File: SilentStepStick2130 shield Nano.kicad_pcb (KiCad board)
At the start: 4 copper layers, 34.5 x 49.4 mm, 8 parts, among them J1 Conn_01x04_Socket, J2 Conn_01x04_Socket, J5 Conn_01x03, U1 TMC2130_SILENTSTEPSTICK, U2 TMC2130_SILENTSTEPSTICK

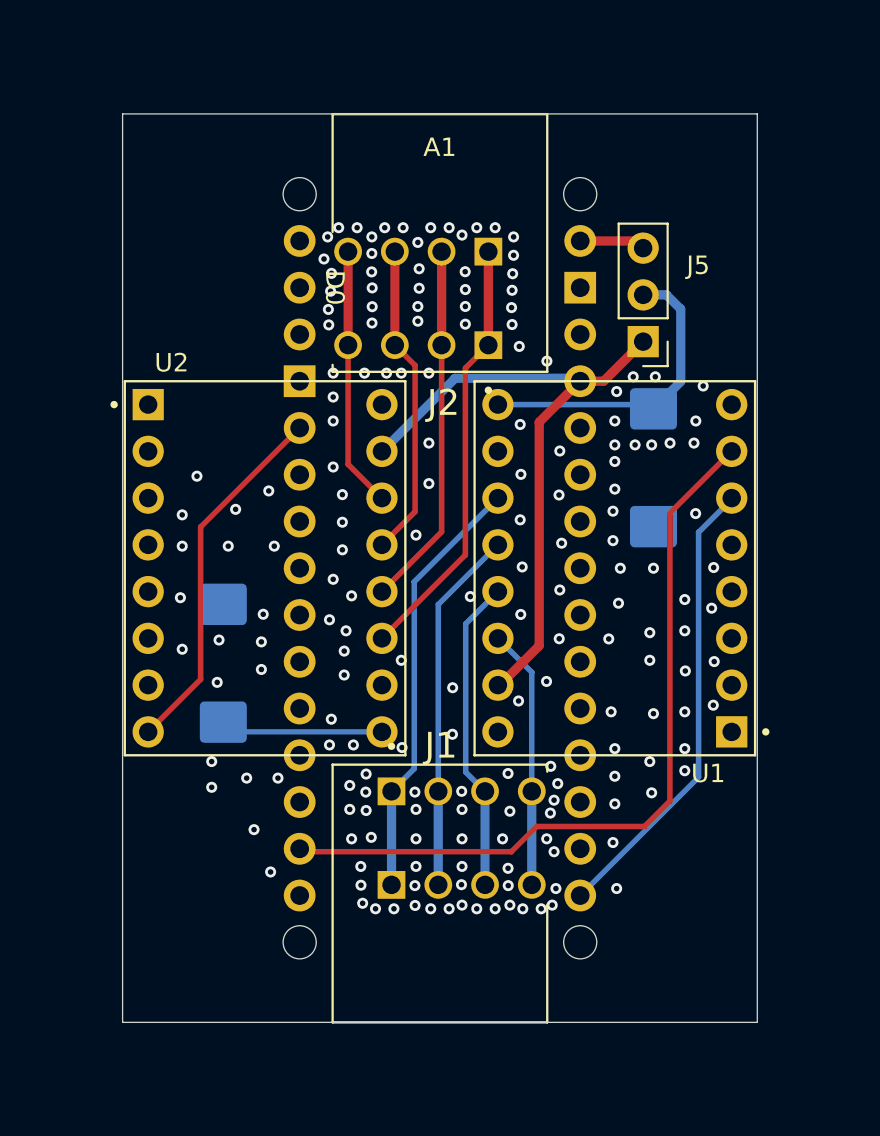
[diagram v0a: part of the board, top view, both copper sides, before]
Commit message: redo, nano on the wrong side (can work with headerless nano)
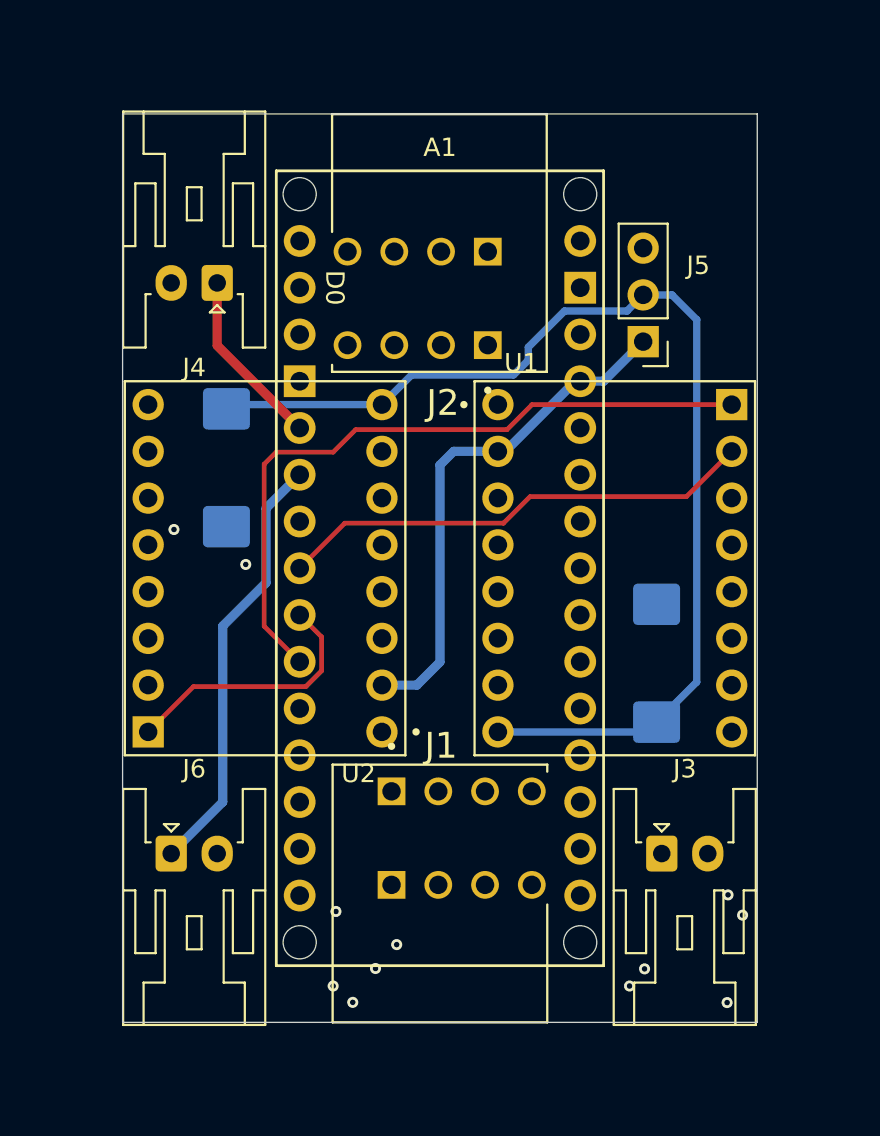
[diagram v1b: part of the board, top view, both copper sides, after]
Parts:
- added J3: Conn_01x02_Pin, Connector_JST:JST_XA_S02B-XASK-1_1x02_P2.50mm_Horizontal, F.Cu at (162.1, 115.5)
- added J4: Conn_01x02_Pin, Connector_JST:JST_XA_S02B-XASK-1_1x02_P2.50mm_Horizontal, F.Cu at (137.9, 84.5)
- added J6: Conn_01x02_Pin, Connector_JST:JST_XA_S02B-XASK-1_1x02_P2.50mm_Horizontal, F.Cu at (135.4, 115.5)
- A1: footprint LibPersoNadj:Arduino_Nano_Every_Shield -> PCM_arduino-library:Arduino_Nano_Every_Socket
- moved C1 23.5 mm to (161.8, 105.2)
- moved C2 23.2 mm to (138.4, 94.5)
- moved A1 21.6 mm to (150.0, 121.6)
- turned U1 to 0 degrees
- turned U2 to 180 degrees
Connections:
- A1 pad D10: unconnected-(A1-PadD10) -> /CS_1
- A1 pad D2: /~{EN_2} -> Net-(J4-Pin_1)
- A1 pad D3: /~{EN_1} -> Net-(J6-Pin_1)
- A1 pad D8: /CS_2 -> Net-(J3-Pin_1)
- A1 pad D9: /CS_1 -> /CS_2
- U1 pad 8: /~{EN_1} -> GND
- U2 pad 8: /~{EN_2} -> GND
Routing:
- net Net-(J3-Pin_1): track 0.00 -> 37.9 mm, vias 0 -> 2
- net /CS_1: track 30.6 -> 58.1 mm, vias 0 -> 2
- net /~{EN_1}: track 26.4 -> 0.00 mm
- net Net-(J6-Pin_1): track 0.00 -> 23.5 mm
- net /~{EN_2}: track 19.9 -> 0.00 mm
- net /VM: track 46.2 -> 60.7 mm
- net /DIR_1: track 25.0 -> 38.3 mm
- net /MISO: track 61.9 -> 75.0 mm, vias 0 -> 2
- net /SCK: track 56.2 -> 68.6 mm, vias 0 -> 2
- net /MOSI: track 55.8 -> 66.8 mm, vias 0 -> 2
- net Net-(J4-Pin_1): track 0.00 -> 9.74 mm
- net /OB2_2: track 14.2 -> 21.8 mm
- net /OA2_2: track 23.4 -> 15.8 mm
- net /OB2_1: track 14.2 -> 21.8 mm
- net /OA2_1: track 23.4 -> 15.8 mm
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
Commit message: v1
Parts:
- added REF**: KiCad-Logo2_5mm_SilkScreen, Symbol:KiCad-Logo2_5mm_SilkScreen, B.Cu at (161.9, 93.6)
- A1: moved to B.Cu
- moved J4 26.7 mm to (164.6, 84.5)
- moved J3 26.7 mm to (135.4, 115.5)
- moved J6 26.7 mm to (162.1, 115.5)
- moved J5 22.1 mm to (139.0, 87.7)
- moved U1 19.0 mm to (140.5, 100.0), turned to 180 degrees
- moved U2 19.0 mm to (159.5, 100.0), turned to 0 degrees
- turned A1 to 180 degrees
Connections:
- J1 pad 1: /OA2_1 -> /OB2_1
- J1 pad 2: /OA1_1 -> /OB1_1
- J1 pad 3: /OB1_1 -> /OA1_1
- J1 pad 4: /OB2_1 -> /OA2_1
- J2 pad 1: /OA2_2 -> /OB2_2
- J2 pad 2: /OA1_2 -> /OB1_2
- J2 pad 3: /OB1_2 -> /OA1_2
- J2 pad 4: /OB2_2 -> /OA2_2
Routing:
- net /MOSI: track 66.8 -> 91.2 mm
- net /CS_1: track 58.1 -> 35.4 mm, vias 2 -> 0
- net /VM: track 60.7 -> 46.8 mm
- net /DIR_1: track 38.3 -> 25.0 mm
- net Net-(J3-Pin_1): track 37.9 -> 26.1 mm, vias 2 -> 0
- net /OA2_2: track 15.8 -> 25.2 mm
- net /OA2_1: track 15.8 -> 25.2 mm
- net +5V: track 28.2 -> 35.5 mm, vias 0 -> 1
- net /OB2_2: track 21.8 -> 15.2 mm
- net /MISO: track 75.0 -> 68.9 mm, vias 2 -> 1
- net /OB2_1: track 21.8 -> 15.8 mm
- net /STEP_2: track 16.0 -> 10.7 mm, vias 1 -> 0
- net /OB1_2: track 21.0 -> 17.2 mm
- net /OB1_1: track 21.0 -> 17.2 mm
- net /OA1_2: track 17.3 -> 20.8 mm
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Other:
- board text added: "v2"
